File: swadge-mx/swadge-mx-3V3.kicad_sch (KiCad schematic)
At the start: 6 parts, among them U4 FM8002A

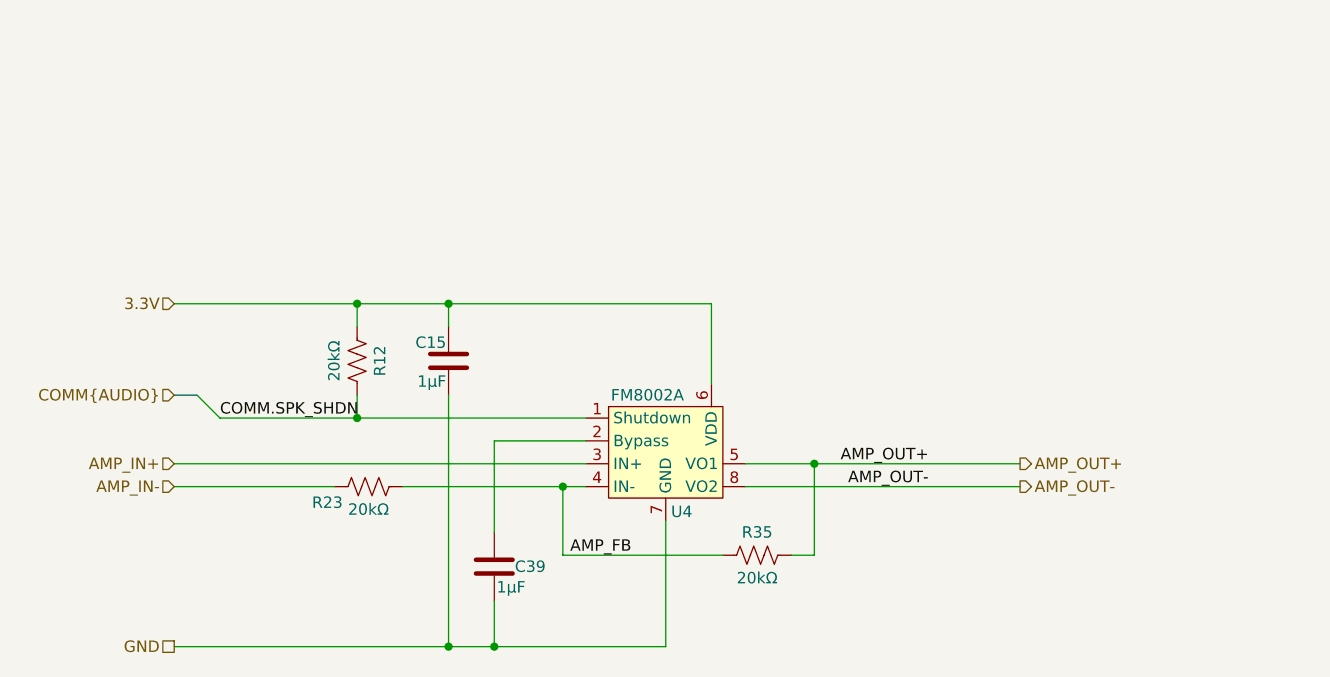
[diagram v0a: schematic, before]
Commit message: Further Subdivide Sheets
Moved all audio into one sheet, and sub-divided into DAC and amp sheets. Moved all power into one sheet and sub-divided into BMS and Buck.
Cleaned up front page a bit.
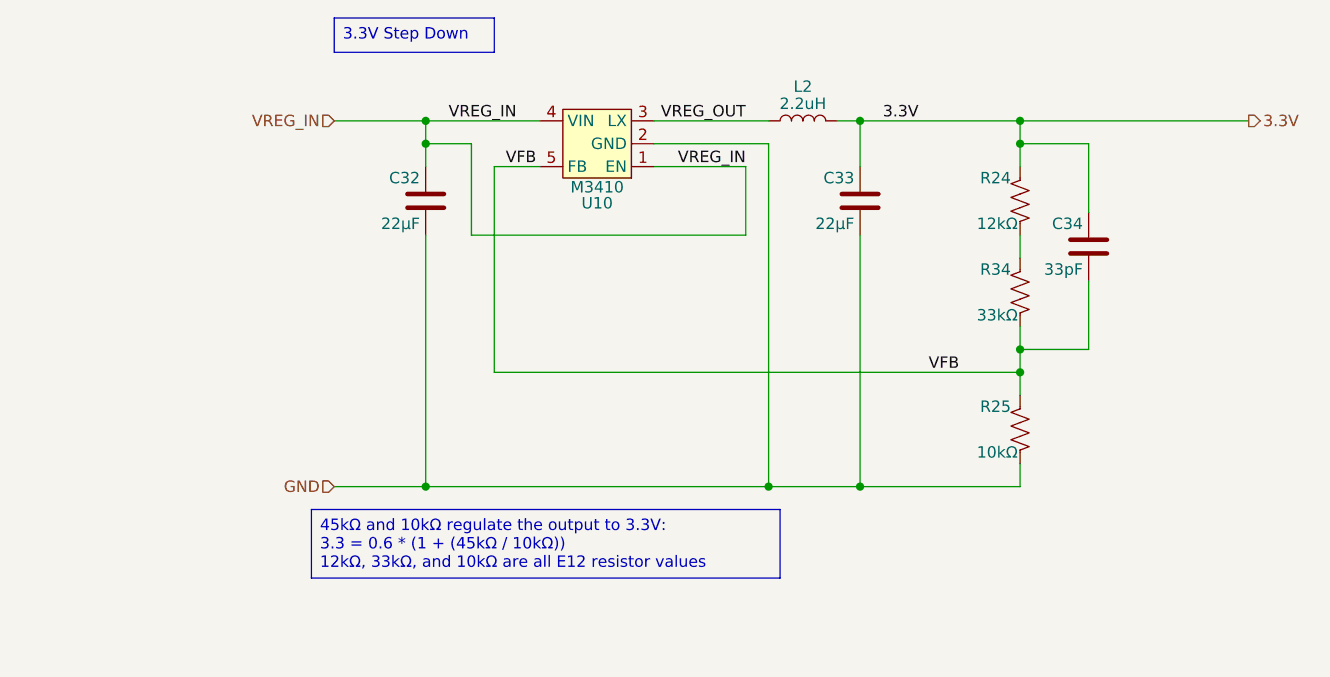
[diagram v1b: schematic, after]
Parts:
- removed C15, C39: 1μF, Swadge_Parts:C_0603_1608Metric, symbol Swadge_Parts:C
- removed R12, R23, R35: 20kΩ, Swadge_Parts:R_0603_1608Metric, symbol Swadge_Parts:R_US
- removed U4: FM8002A, Swadge_Parts:SOP-8_3.9x4.9mm_P1.27mm, symbol Swadge_Parts:FM8002A
- added C32, C33: 22μF, Swadge_Parts:C_0603_1608Metric, symbol Swadge_Parts:C
- added C34: 33pF, Swadge_Parts:C_0603_1608Metric, symbol Swadge_Parts:C
- added L2: 2.2uH, Swadge_Parts:L_1008_2520Metric, symbol Swadge_Parts:L
- added R24: 12kΩ, Swadge_Parts:R_0603_1608Metric, symbol Swadge_Parts:R_US
- added R25: 10kΩ, Swadge_Parts:R_0603_1608Metric, symbol Swadge_Parts:R_US
- added R34: 33kΩ, Swadge_Parts:R_0603_1608Metric, symbol Swadge_Parts:R_US
- added U10: M3410, Swadge_Parts:SOT-23-5, symbol Swadge_Parts:M3410
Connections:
- net 3.3V: now also C33.1, C34.1, L2.1, R24.1
- net GND: now also C32.2, C33.2, R25.2, U10.2 (GND)
- new net: R24.2, R34.1
- new net VFB: C34.2, R25.1, R34.2, U10.5 (FB)
- new net VREG_IN: C32.1, U10.1 (EN), U10.4 (VIN)
- new net VREG_OUT: L2.2, U10.3 (LX)
